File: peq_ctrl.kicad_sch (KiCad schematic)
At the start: 40 parts, among them J5 DC_IN, J7 INPUT, J8 OUTPUT, Q1 2N3904, SW2 HIGH_FREQ_SW, SW3 LOW_FREQ_SW, SW4 SW_SPDT, U1 NJM4580

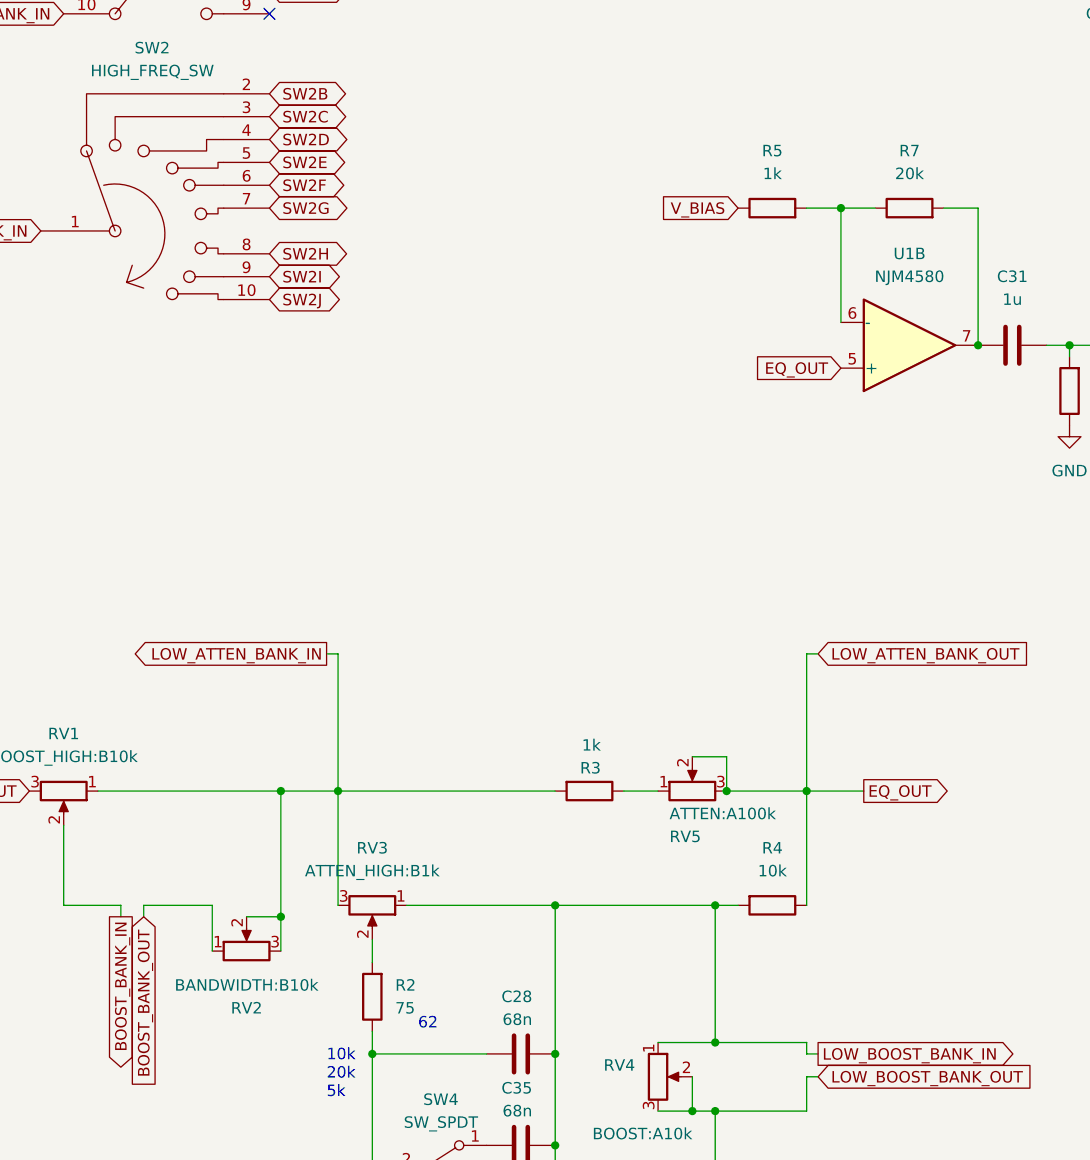
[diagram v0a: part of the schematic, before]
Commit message: change values: R7 to 47k, RV2 to B5k
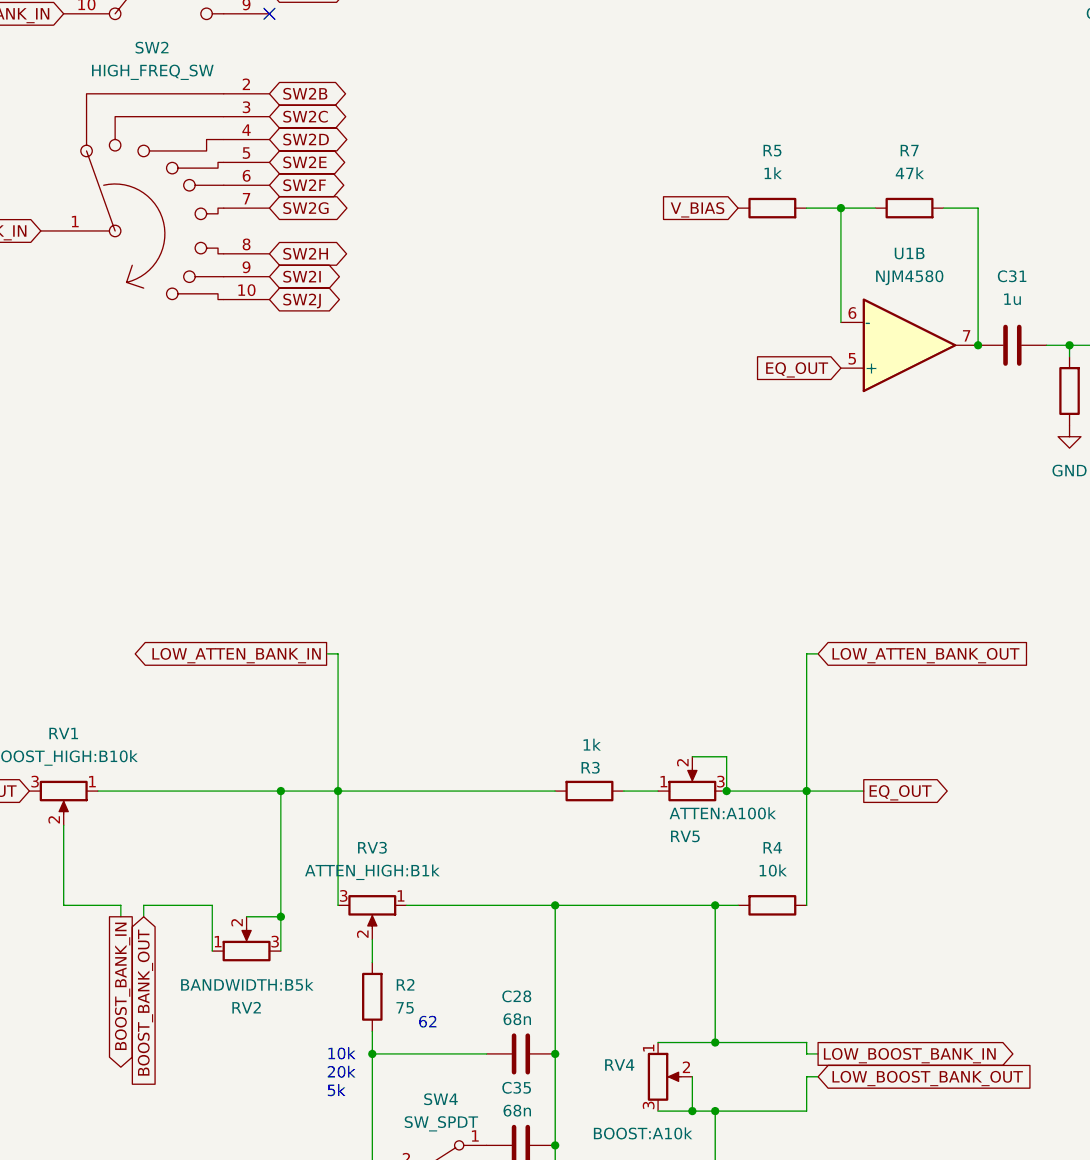
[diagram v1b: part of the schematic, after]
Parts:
- R7: value 20k -> 47k
- RV2: value BANDWIDTH:B10k -> BANDWIDTH:B5k
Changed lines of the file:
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@@
     (in_bom yes) (on_board yes) (fields_autoplaced)
     (property "Reference" "R7" (id 0) (at 129.54 64.77 90))
-    (property "Value" "20k" (id 1) (at 129.54 67.31 90))
+    (property "Value" "47k" (id 1) (at 129.54 67.31 90))
     (property "Footprint" "ak_misc:R_Axial_DIN0207_L6.3mm_D2.5mm_P7.62mm_with_SMD" (id 2) (at 129.54 72.898 90)
       (effects (font (size 1.27 1.27)) hide)
@@
     (in_bom yes) (on_board yes)
     (property "Reference" "RV2" (id 0) (at 55.88 160.02 90))
-    (property "Value" "BANDWIDTH:B10k" (id 1) (at 55.88 157.48 90))
+    (property "Value" "BANDWIDTH:B5k" (id 1) (at 55.88 157.48 90))
     (property "Footprint" "ak_misc:POT-16mm" (id 2) (at 55.88 153.67 0)
       (effects (font (size 1.27 1.27)) hide)

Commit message: add protection components and fix layout
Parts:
- added C37: NC, Capacitor_SMD:C_0805_2012Metric_Pad1.18x1.45mm_HandSolder, symbol Device:C
- added C38, C39: 0.1u, Capacitor_SMD:C_0805_2012Metric_Pad1.18x1.45mm_HandSolder, symbol Device:C
- added D1: LED, LED_THT:LED_D3.0mm, symbol Device:LED
- added D3: D_Zener, Diode_THT:D_DO-35_SOD27_P2.54mm_Vertical_AnodeUp, symbol Device:D_Zener
- added F1: Polyfuse, Resistor_THT:R_Axial_DIN0204_L3.6mm_D1.6mm_P5.08mm_Horizontal, symbol Device:Polyfuse
- added R1: 47k, ak_misc:R_Axial_DIN0207_L6.3mm_D2.5mm_P7.62mm_with_SMD, symbol Device:R
- added R10, R9: 470k, Resistor_SMD:R_0805_2012Metric_Pad1.20x1.40mm_HandSolder, symbol Device:R
- added SW1: 3PDT_FootSwitch, ak_misc:3PDT_FootSwitch_ovalpad, symbol ak_misc:3PDT_FootSwitch
- D2: footprint Diode_THT:D_DO-34_SOD68_P7.62mm_Horizontal -> Diode_THT:D_DO-35_SOD27_P7.62mm_Horizontal
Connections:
- net +VDC: now also R1.2
- net GND: now also C38.1, C39.1, D3.2 (A), SW1.4
- net INPUT: now also SW1.7
- net INPUT_JACK: now also SW1.8
- net LOW_ATTEN_BANK_IN: now also RN1.4 (R4.1)
- net OUTPUT: now also SW1.1
- net OUTPUT_JACK: now also SW1.2
- net at C31.1, R7.2, U1.7: now also C37.2
- net at D2.2 (A), JP2.1 (A): now also D3.1 (K), F1.2; no longer J5.2
- net at C30.1, D2.1 (K), JP2.2 (B)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: now also C38.2
- net at C34.1, Q1.2 (B), R26.1: now also C39.2
- net at C36.1, SW4.3 (C): now also R10.1
- net at C28.1, R2.1, SW4.2 (B): now also R10.2, R9.2
- net at R5.2, R7.1, U1.6 (-): now also C37.1
- net at C35.1, SW4.1 (A): now also R9.1
- new net: SW1.3, SW1.9
- new net: F1.1, J5.2
- new net: D1.2 (A), R1.1
- new net: D1.1 (K), SW1.5
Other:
- moved on the sheet: C30, C31, C34, C35, C36, D2, J5, J8, JP2, JP3, Q1, R26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

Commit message: update comments and credits
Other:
- note added: "60"
- note removed: "80"
- company: (none) -> MST/mesotokyo
- title: (none) -> PEQ
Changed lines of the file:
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@@
 (kicad_sch (version 20211123) (generator eeschema)
   (paper "A4")
+  (title_block
+    (title "PEQ")
+    (date "2024-11-02")
+    (rev "v1.1")
+    (company "MST/mesotokyo")
+    (comment 1 "https://meso.tokyo/")
+  )
   (junction (at 107.95 171.45) (diameter 0) (color 0 0 0 0)
   )
@@
     (effects (font (size 1.27 1.27)) (justify left bottom))
   )
-  (text "80" (at 67.31 30.48 0)
+  (text "60" (at 67.31 30.48 0)
     (effects (font (size 1.27 1.27)) (justify left bottom))
   )
